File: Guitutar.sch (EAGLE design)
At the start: 16 parts

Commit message: Added headers, Bluetooth, ICSP header, and I/O connections
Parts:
- removed JP5: (no value), pinhead:PINHD-2X13
- added C8: (no value), rcl:C-USC0805
- added ICSP: (no value), pinhead:PINHD-2X3
- added LED1: (no value), led:LEDSMT1206
- added R3: (no value), rcl:R-US_M0805
- JP1: device pinhead:PINHD-2X3 -> pinhead:PINHD-1X25
- JP2, JP3, JP4: device pinhead:PINHD-2X13 -> pinhead:PINHD-1X25
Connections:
- removed net GND: C1.2, C7.1
- removed net N$11: C6.2, U$1.VSS5
- removed net N$6: C3.1, U$1.AVSS
- removed net N$8: C5.1, U$1.VSS4
- new net EAN: U$2.EAN
- new net LED: LED1.C, U$2.LED1
- new net N$15: LED1.A, R3.1
- new net N$16: R3.2, U$2.LDO33_O, U$2.VDD_IO
- new net P0_0: JP1.14, JP1.18, U$1.AN19/C2INC/RPG9/PMA2/RG9, U$1.AN32/RPE8/RE8, U$2.P0_0
- new net P0_4: JP1.3, U$1.AN22/RPE5/PMD5/RE5, U$2.P0_4
- new net P0_5: JP1.12, U$1.AN18/C2IND/RPG8/PMA3/RG8, U$2.P0_5
- new net P1_2: U$2.P1_2/SCL
- new net P1_3: U$2.P1_3/SDA
- new net P1_5: JP1.1, U$1.AN28/RG15, U$2.P1_5
- new net P1_7: JP1.19, U$1.AN33/RPE9/RE9, U$2.P1_7
- new net P2_0: U$2.P2_0
- new net P2_4: U$2.P2_4
- new net P3_1: JP1.11, U$1.AN17/C1INC/RPG7/PMA4/RG7, U$2.P3_1
- new net P3_2: JP1.10, U$1.AN16/C1IND/RPG6/SCK2/PMA5/RG6, U$2.P3_2
- new net P3_3: JP1.9, U$1.RPC4/CTED7/RC4, U$2.P3_3
- new net P3_4: JP1.8, U$1.AN31/RPC3/RC3, U$2.P3_4
- new net P3_6: U$2.P3_6
- new net P3_7: JP1.7, U$1.AN30/RPC2/RC2, U$2.P3_7
- new net PE: C1.2, C7.1, C8.2, U$2.GND, U$2.GND1
- new net RST_N: JP1.6, U$1.AN29/RPC1/RC1, U$2.RST_N
- new net RXD: JP1.21, U$1.AN4/C1INB/RB4, U$2.HCI_RXD
- new net SW_BTN: JP1.4, U$1.AN23/PMD6/RE6, U$2.SW_BTN
- new net TXD: JP1.20, U$1.AN5/C1INA/RPB5/VBUSON/RB5, U$2.HCI_TXD
- new net VSS: C2.1, C3.2, C4.2, C5.1, C6.2, JP1.15, JP2.20, JP2.6, JP3.15, JP3.25, U$1.AVSS, U$1.VSS1, U$1.VSS3, U$1.VSS4, U$1.VSS5
- new net WAKEUP: JP1.5, U$1.AN27/PMD7/RE7, U$2.WAKEUP
- net N$10: now also JP4.11
- net N$12: now also JP4.10
- net N$13: now also ICSP.1, JP1.13; no longer JP1.1
- net N$14: now also ICSP.4, JP1.25; no longer JP1.4
- net N$2: now also ICSP.5, JP1.24; no longer JP1.5
- net N$3: now also JP1.17, U$1.TMS/CTED1/RA0; no longer C2.1, U$1.VSS1
- net N$4: now also JP1.22, U$1.PGED3/AN3/C2INA/RPB3/RB3; no longer C4.2, U$1.VSS3
- net N$5: now also JP1.23, U$1.PGEC3/AN2/CTCMP/C2INB/RPB2/CTED13/RB2; no longer C2.2, C3.2, U$1.AVDD, U$1.VDD1
- net N$7: now also JP2.21
- net N$9: now also JP3.12, JP3.5
- net VDD: now also C2.2, C3.1, C8.1, JP1.16, JP1.2, JP2.5, U$1.AVDD, U$1.VDD, U$1.VDD1, U$2.BAT_IN

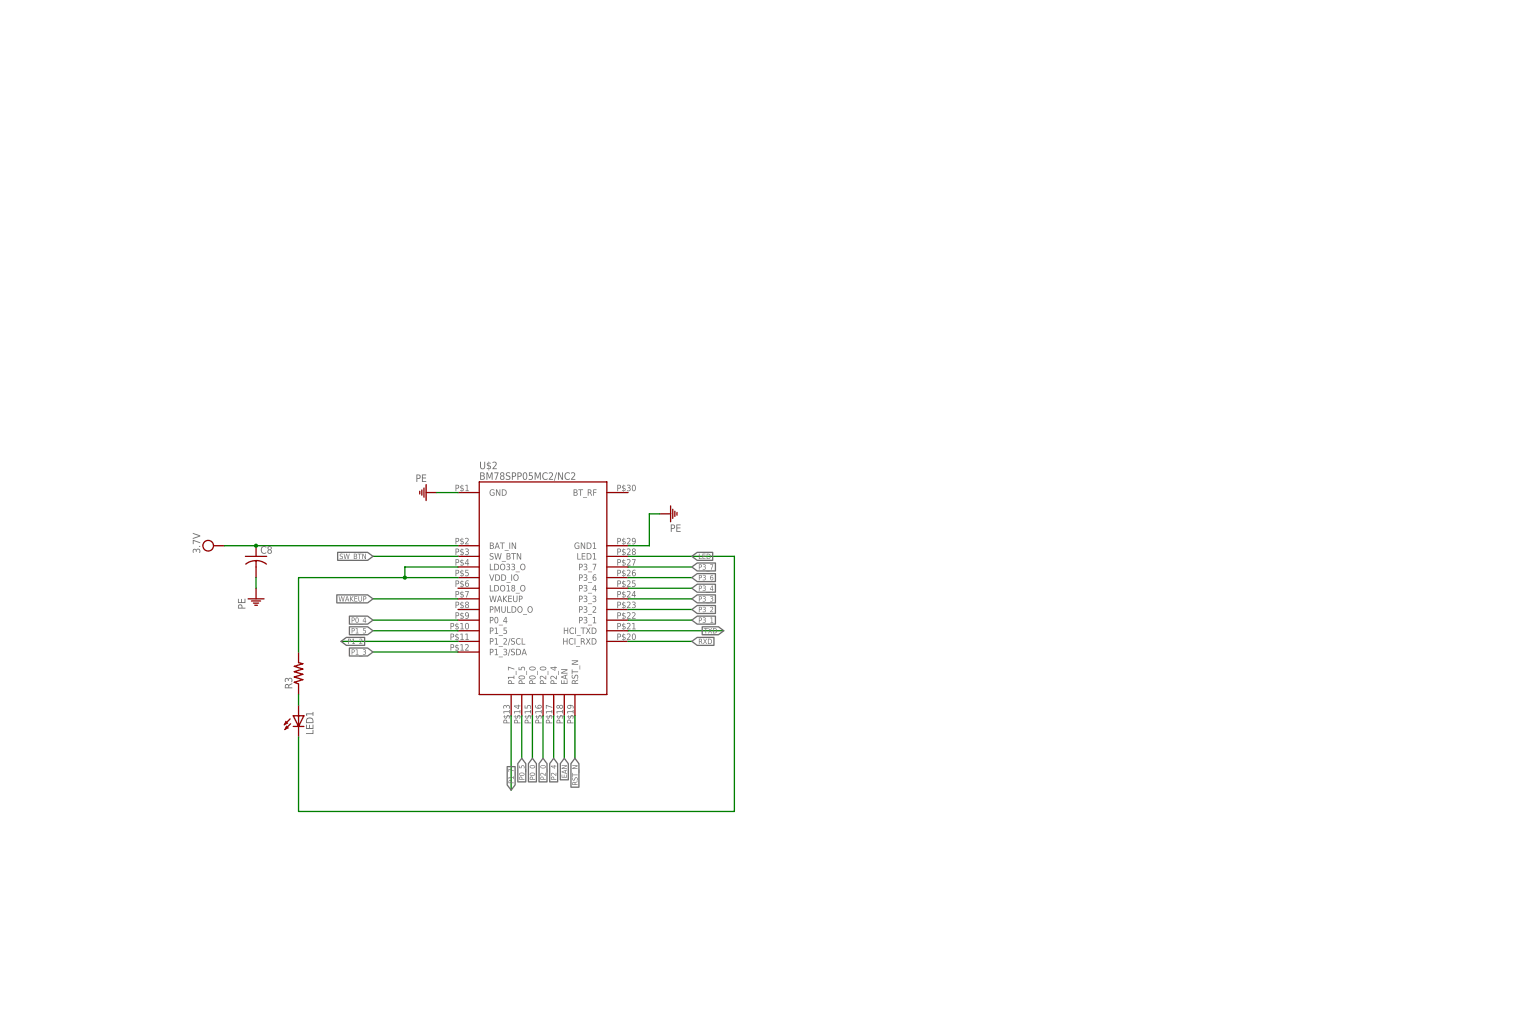
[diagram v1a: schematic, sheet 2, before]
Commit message: Added xref connections, switch matrix, and connected all MCU pins to headers
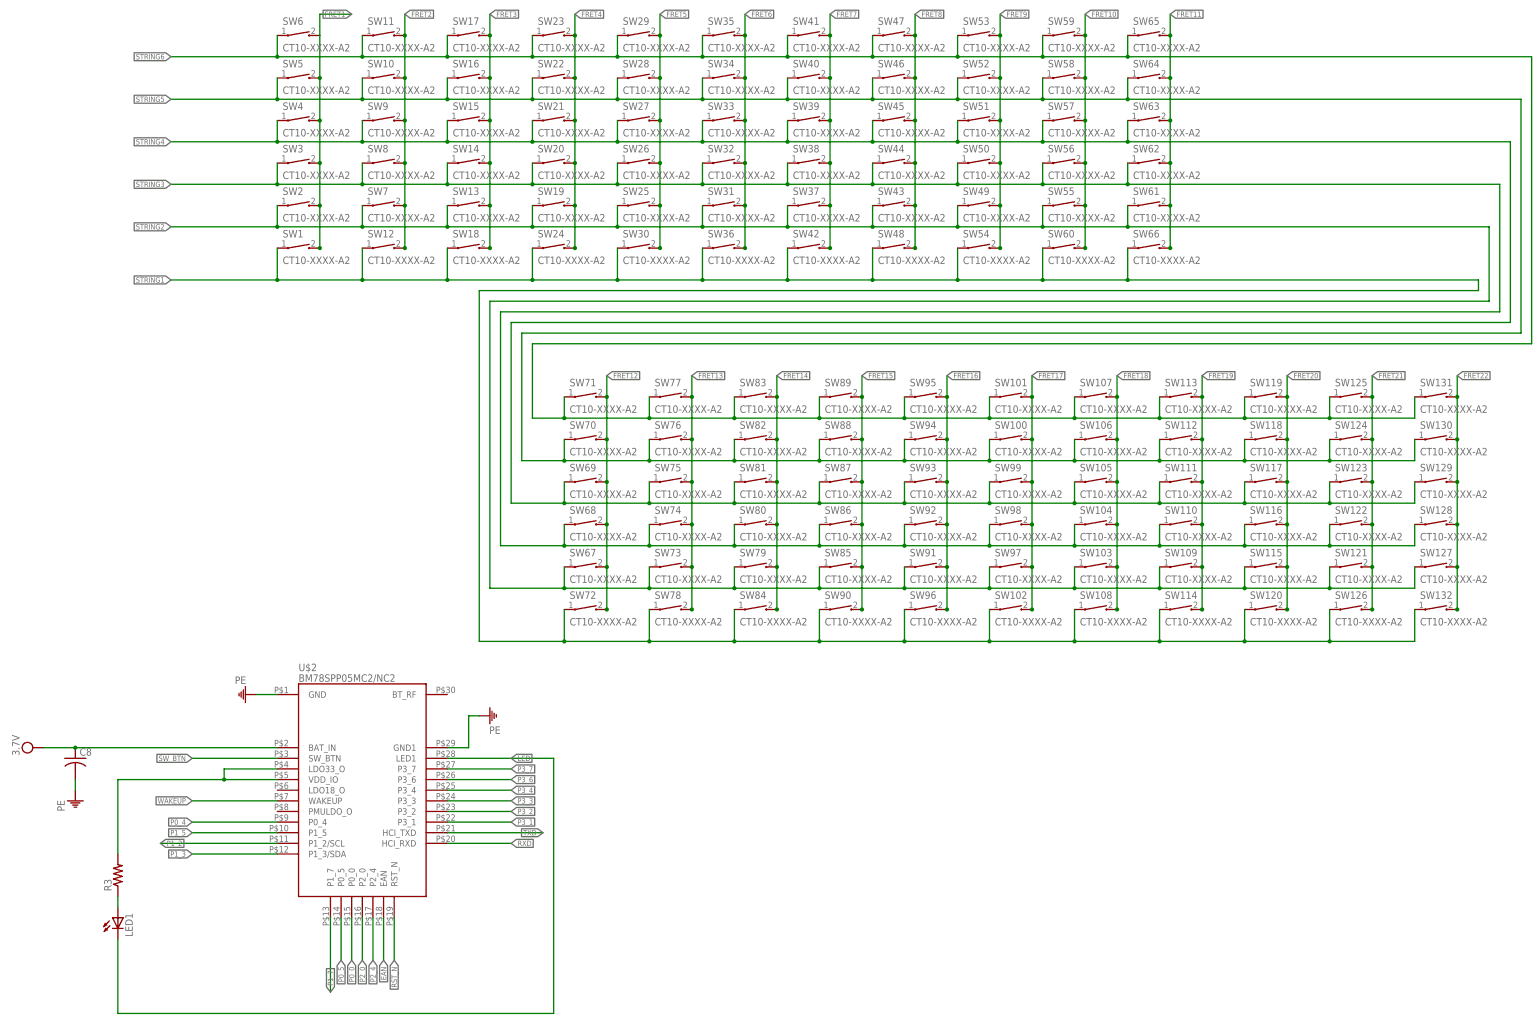
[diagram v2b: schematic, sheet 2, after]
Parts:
- added SW1, SW10, SW100, SW101, SW102, SW103, SW104, SW105, SW106, SW107, SW108, SW109, SW11, SW110, SW111, SW112, SW113, SW114, SW115, SW116, SW117, SW118, SW119, SW12, SW120, SW121, SW122, SW123, SW124, SW125, SW126, SW127, SW128, SW129, SW13, SW130, SW131, SW132, SW14, SW15, SW16, SW17, SW18, SW19, SW2, SW20, SW21, SW22, SW23, SW24, SW25, SW26, SW27, SW28, SW29, SW3, SW30, SW31, SW32, SW33, SW34, SW35, SW36, SW37, SW38, SW39, SW4, SW40, SW41, SW42, SW43, SW44, SW45, SW46, SW47, SW48, SW49, SW5, SW50, SW51, SW52, SW53, SW54, SW55, SW56, SW57, SW58, SW59, SW6, SW60, SW61, SW62, SW63, SW64, SW65, SW66, SW67, SW68, SW69, SW7, SW70, SW71, SW72, SW73, SW74, SW75, SW76, SW77, SW78, SW79, SW8, SW80, SW81, SW82, SW83, SW84, SW85, SW86, SW87, SW88, SW89, SW9, SW90, SW91, SW92, SW93, SW94, SW95, SW96, SW97, SW98, SW99: CT10-XXXX-A2, switch-coto:CT10-XXXX-A2
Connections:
- new net FRET1: JP2.16, SW1.2, SW2.2, SW3.2, SW4.2, SW5.2, SW6.2, U$1.AN12/PMA11/RB12
- new net FRET10: JP3.2, SW55.2, SW56.2, SW57.2, SW58.2, SW59.2, SW60.2, U$1.AN38/RPF2/RF2
- new net FRET11: JP3.3, SW61.2, SW62.2, SW63.2, SW64.2, SW65.2, SW66.2, U$1.AN39/RPF8/RF8
- new net FRET12: JP3.8, SW67.2, SW68.2, SW69.2, SW70.2, SW71.2, SW72.2, U$1.SCL2/RA2
- new net FRET13: JP3.9, SW73.2, SW74.2, SW75.2, SW76.2, SW77.2, SW78.2, U$1.SDA2/RA3
- new net FRET14: JP3.10, SW79.2, SW80.2, SW81.2, SW82.2, SW83.2, SW84.2, U$1.TDI/CTED9/RA4
- new net FRET15: JP3.11, SW85.2, SW86.2, SW87.2, SW88.2, SW89.2, SW90.2, U$1.TDO/RA5
- new net FRET16: JP3.13, SW91.2, SW92.2, SW93.2, SW94.2, SW95.2, SW96.2, U$1.OSC1/CLKI/RC12
- new net FRET17: JP3.14, SW100.2, SW101.2, SW102.2, SW97.2, SW98.2, SW99.2, U$1.OSC2/CLKO/RC15
- new net FRET18: JP3.16, SW103.2, SW104.2, SW105.2, SW106.2, SW107.2, SW108.2, U$1.RPA14/SCL1/RA14
- new net FRET19: JP3.17, SW109.2, SW110.2, SW111.2, SW112.2, SW113.2, SW114.2, U$1.RPA15/SDA1/RA15
- new net FRET2: JP2.17, SW10.2, SW11.2, SW12.2, SW7.2, SW8.2, SW9.2, U$1.AN13/PMA10/RB13
- new net FRET20: JP3.18, SW115.2, SW116.2, SW117.2, SW118.2, SW119.2, SW120.2, U$1.RPD8/RTCC/RD8
- new net FRET21: JP3.19, SW121.2, SW122.2, SW123.2, SW124.2, SW125.2, SW126.2, U$1.RPD9/RD9
- new net FRET22: JP3.20, SW127.2, SW128.2, SW129.2, SW130.2, SW131.2, SW132.2, U$1.RPD10/SCK1/PMA15/RD10
- new net FRET3: JP2.18, SW13.2, SW14.2, SW15.2, SW16.2, SW17.2, SW18.2, U$1.AN14/RPB14/CTED5/PMA1/RB14
- new net FRET4: JP2.19, SW19.2, SW20.2, SW21.2, SW22.2, SW23.2, SW24.2, U$1.AN15/RPB15/OCFB/CTED6/PMA0/RB15
- new net FRET5: JP2.22, SW25.2, SW26.2, SW27.2, SW28.2, SW29.2, SW30.2, U$1.AN36/RPD14/RD14
- new net FRET6: JP2.23, SW31.2, SW32.2, SW33.2, SW34.2, SW35.2, SW36.2, U$1.AN37/RPD15/SCK4/RD15
- new net FRET7: JP2.24, SW37.2, SW38.2, SW39.2, SW40.2, SW41.2, SW42.2, U$1.RPF4/PMA9/RF4
- new net FRET8: JP2.25, SW43.2, SW44.2, SW45.2, SW46.2, SW47.2, SW48.2, U$1.RPF5/PMA8/RF5
- new net FRET9: JP3.1, SW49.2, SW50.2, SW51.2, SW52.2, SW53.2, SW54.2, U$1.USBID/RPF3/RF3
- new net N$100: JP4.19, U$1.AN47/PMD1/RE1
- new net N$101: JP4.20, U$1.RG14
- new net N$102: JP4.21, U$1.RG12
- new net N$103: JP4.22, U$1.RG13
- new net N$104: JP4.23, U$1.AN20/PMD2/RE2
- new net N$105: JP4.24, U$1.RPE3/CTPLS/PMD3/RE3
- new net N$106: JP4.25, U$1.AN21/PMD4/RE4
- new net N$42: JP2.1, U$1.PGEC2/AN6/RPB6/RB6
- new net N$43: JP2.2, U$1.PGED2/AN7/RPB7/CTED3/RB7
- new net N$44: JP2.3, U$1.VREF-/PMA7/RA9
- new net N$45: JP2.4, U$1.VREF+/PMA6/RA10
- new net N$50: JP2.11, U$1.VSS2
- new net N$51: JP2.12, U$1.VDD2
- new net N$52: JP2.13, U$1.TCK/CTED2/RA1
- new net N$66: JP3.4, U$1.VBUS
- new net N$67: JP3.6, U$1.D-
- new net N$68: JP3.7, U$1.D+
- new net N$80: JP3.21, U$1.RPD11/PMA14/RD11
- new net N$81: JP3.22, U$1.RPD0/INT0/RD0
- new net N$82: JP3.23, U$1.SOSCI/RPC13/RC13
- new net N$83: JP3.24, U$1.SOSCO/RPC14/T1CK/RC14
- new net N$84: JP4.1, U$1.AN24/RPD1/RD1
- new net N$85: JP4.2, U$1.AN25/RPD2/RD2
- new net N$86: JP4.3, U$1.AN26/C3IND/RPD3/RD3
- new net N$87: JP4.4, U$1.AN40/RPD12/PMD12/RD12
- new net N$88: JP4.5, U$1.AN41/PMD13/RD13
- new net N$89: JP4.6, U$1.RPD4/PMWR/RD4
- new net N$90: JP4.7, U$1.RPD5/PMRD/RD5
- new net N$91: JP4.8, U$1.AN42/C3INC/PMD14/RD6
- new net N$92: JP4.9, U$1.AN43/C3INB/PMD15/RD7
- new net N$93: JP4.12, U$1.AN44/C3INA/RPF0/PMD11/RF0
- new net N$94: JP4.13, U$1.AN45/RPF1/PMD10/RF1
- new net N$95: JP4.14, U$1.RPG1/PMD9/RG1
- new net N$96: JP4.15, U$1.RPG0/PMD8/RG0
- new net N$97: JP4.16, U$1.RA6
- new net N$98: JP4.17, U$1.CTED8/RA7
- new net N$99: JP4.18, U$1.AN46/PMD0/RE0
- new net STRING1: JP2.7, SW1.1, SW102.1, SW108.1, SW114.1, SW12.1, SW120.1, SW126.1, SW132.1, SW18.1, SW24.1, SW30.1, SW36.1, SW42.1, SW48.1, SW54.1, SW60.1, SW66.1, SW72.1, SW78.1, SW84.1, SW90.1, SW96.1, U$1.AN8/RPB8/CTED10/RB8
- new net STRING2: JP2.8, SW103.1, SW109.1, SW115.1, SW121.1, SW127.1, SW13.1, SW19.1, SW2.1, SW25.1, SW31.1, SW37.1, SW43.1, SW49.1, SW55.1, SW61.1, SW67.1, SW7.1, SW73.1, SW79.1, SW85.1, SW91.1, SW97.1, U$1.AN9/RPB9/CTED4/RB9
- new net STRING3: JP2.9, SW104.1, SW110.1, SW116.1, SW122.1, SW128.1, SW14.1, SW20.1, SW26.1, SW3.1, SW32.1, SW38.1, SW44.1, SW50.1, SW56.1, SW62.1, SW68.1, SW74.1, SW8.1, SW80.1, SW86.1, SW92.1, SW98.1, U$1.CVREFOUT/AN10/RPB10/CTED11/PMA13/RB10
- new net STRING4: JP2.10, SW105.1, SW111.1, SW117.1, SW123.1, SW129.1, SW15.1, SW21.1, SW27.1, SW33.1, SW39.1, SW4.1, SW45.1, SW51.1, SW57.1, SW63.1, SW69.1, SW75.1, SW81.1, SW87.1, SW9.1, SW93.1, SW99.1, U$1.AN11/PMA12/RB11
- new net STRING5: JP2.14, SW10.1, SW100.1, SW106.1, SW112.1, SW118.1, SW124.1, SW130.1, SW16.1, SW22.1, SW28.1, SW34.1, SW40.1, SW46.1, SW5.1, SW52.1, SW58.1, SW64.1, SW70.1, SW76.1, SW82.1, SW88.1, SW94.1, U$1.AN34/RPF13/SCK3/RF13
- new net STRING6: JP2.15, SW101.1, SW107.1, SW11.1, SW113.1, SW119.1, SW125.1, SW131.1, SW17.1, SW23.1, SW29.1, SW35.1, SW41.1, SW47.1, SW53.1, SW59.1, SW6.1, SW65.1, SW71.1, SW77.1, SW83.1, SW89.1, SW95.1, U$1.AN35/RPF12/RF12
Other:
- moved on the sheet: C3, C4, C5, C6, C7, C8, LED1, R3, U$2

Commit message: Added LEDs and connected them to MCU. Increased size of page 2.
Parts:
- added LED10, LED100, LED101, LED102, LED103, LED104, LED105, LED106, LED107, LED108, LED109, LED11, LED110, LED111, LED112, LED113, LED114, LED115, LED116, LED117, LED118, LED119, LED12, LED120, LED121, LED122, LED123, LED124, LED125, LED126, LED127, LED128, LED129, LED13, LED130, LED131, LED132, LED133, LED134, LED135, LED136, LED137, LED138, LED139, LED14, LED15, LED16, LED17, LED18, LED19, LED2, LED20, LED21, LED22, LED23, LED24, LED25, LED26, LED27, LED28, LED29, LED3, LED30, LED31, LED32, LED33, LED34, LED35, LED36, LED37, LED38, LED39, LED4, LED40, LED41, LED42, LED43, LED44, LED45, LED46, LED47, LED48, LED49, LED5, LED50, LED51, LED52, LED53, LED54, LED55, LED56, LED57, LED58, LED59, LED6, LED60, LED61, LED62, LED63, LED64, LED65, LED66, LED67, LED68, LED69, LED7, LED70, LED71, LED72, LED73, LED74, LED75, LED76, LED77, LED78, LED79, LED8, LED80, LED81, LED82, LED83, LED84, LED85, LED86, LED87, LED88, LED89, LED9, LED90, LED91, LED92, LED93, LED94, LED95, LED96, LED97, LED98, LED99: (no value), led:LEDSMT1206
- added U$10, U$11, U$12, U$13, U$14, U$15, U$16, U$17, U$18, U$19, U$20, U$21, U$22, U$23, U$24, U$25, U$3, U$4, U$5, U$6, U$7, U$8, U$9: MM74HC595TSSOP-LD16, ECE477_Guitutar:MM74HC595TSSOP-LD16
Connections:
- removed net N$100: JP4.19, U$1.AN47/PMD1/RE1
- removed net N$101: JP4.20, U$1.RG14
- removed net N$102: JP4.21, U$1.RG12
- removed net N$103: JP4.22, U$1.RG13
- removed net N$104: JP4.23, U$1.AN20/PMD2/RE2
- removed net N$105: JP4.24, U$1.RPE3/CTPLS/PMD3/RE3
- removed net N$106: JP4.25, U$1.AN21/PMD4/RE4
- removed net N$80: JP3.21, U$1.RPD11/PMA14/RD11
- removed net N$81: JP3.22, U$1.RPD0/INT0/RD0
- removed net N$82: JP3.23, U$1.SOSCI/RPC13/RC13
- removed net N$83: JP3.24, U$1.SOSCO/RPC14/T1CK/RC14
- removed net N$84: JP4.1, U$1.AN24/RPD1/RD1
- removed net N$85: JP4.2, U$1.AN25/RPD2/RD2
- removed net N$86: JP4.3, U$1.AN26/C3IND/RPD3/RD3
- removed net N$87: JP4.4, U$1.AN40/RPD12/PMD12/RD12
- removed net N$88: JP4.5, U$1.AN41/PMD13/RD13
- removed net N$89: JP4.6, U$1.RPD4/PMWR/RD4
- removed net N$90: JP4.7, U$1.RPD5/PMRD/RD5
- removed net N$91: JP4.8, U$1.AN42/C3INC/PMD14/RD6
- removed net N$92: JP4.9, U$1.AN43/C3INB/PMD15/RD7
- removed net N$93: JP4.12, U$1.AN44/C3INA/RPF0/PMD11/RF0
- removed net N$94: JP4.13, U$1.AN45/RPF1/PMD10/RF1
- removed net N$95: JP4.14, U$1.RPG1/PMD9/RG1
- removed net N$96: JP4.15, U$1.RPG0/PMD8/RG0
- removed net N$97: JP4.16, U$1.RA6
- removed net N$98: JP4.17, U$1.CTED8/RA7
- removed net N$99: JP4.18, U$1.AN46/PMD0/RE0
- new net G: JP3.24, U$1.SOSCO/RPC14/T1CK/RC14, U$10.G, U$11.G, U$12.G, U$13.G, U$14.G, U$15.G, U$16.G, U$17.G, U$18.G, U$19.G, U$20.G, U$21.G, U$22.G, U$23.G, U$24.G, U$25.G, U$3.G, U$4.G, U$5.G, U$6.G, U$7.G, U$8.G, U$9.G
- new net GND: LED10.C, LED100.C, LED101.C, LED102.C, LED103.C, LED104.C, LED105.C, LED106.C, LED107.C, LED108.C, LED109.C, LED11.C, LED110.C, LED111.C, LED112.C, LED113.C, LED114.C, LED115.C, LED116.C, LED117.C, LED118.C, LED119.C, LED12.C, LED120.C, LED121.C, LED122.C, LED123.C, LED124.C, LED125.C, LED126.C, LED127.C, LED128.C, LED129.C, LED13.C, LED130.C, LED131.C, LED132.C, LED133.C, LED134.C, LED135.C, LED136.C, LED137.C, LED138.C, LED139.C, LED14.C, LED15.C, LED16.C, LED17.C, LED18.C, LED19.C, LED2.C, LED20.C, LED21.C, LED22.C, LED23.C, LED24.C, LED25.C, LED26.C, LED27.C, LED28.C, LED29.C, LED3.C, LED30.C, LED31.C, LED32.C, LED33.C, LED34.C, LED35.C, LED36.C, LED37.C, LED38.C, LED39.C, LED4.C, LED40.C, LED41.C, LED42.C, LED43.C, LED44.C, LED45.C, LED46.C, LED47.C, LED48.C, LED49.C, LED5.C, LED50.C, LED51.C, LED52.C, LED53.C, LED54.C, LED55.C, LED56.C, LED57.C, LED58.C, LED59.C, LED6.C, LED60.C, LED61.C, LED62.C, LED63.C, LED64.C, LED65.C, LED66.C, LED67.C, LED68.C, LED69.C, LED7.C, LED70.C, LED71.C, LED72.C, LED73.C, LED74.C, LED75.C, LED76.C, LED77.C, LED78.C, LED79.C, LED8.C, LED80.C, LED81.C, LED82.C, LED83.C, LED84.C, LED85.C, LED86.C, LED87.C, LED88.C, LED89.C, LED9.C, LED90.C, LED91.C, LED92.C, LED93.C, LED94.C, LED95.C, LED96.C, LED97.C, LED98.C, LED99.C, U$10.GND, U$11.GND, U$12.GND, U$13.GND, U$14.GND, U$15.GND, U$16.GND, U$17.GND, U$18.GND, U$19.GND, U$20.GND, U$21.GND, U$22.GND, U$23.GND, U$24.GND, U$25.GND, U$3.GND, U$4.GND, U$5.GND, U$6.GND, U$7.GND, U$8.GND, U$9.GND
- new net LED_SER1: JP4.25, U$1.AN21/PMD4/RE4, U$3.SER
- new net LED_SER10: JP4.16, U$1.RA6, U$12.SER
- new net LED_SER11: JP4.15, U$1.RPG0/PMD8/RG0, U$13.SER
- new net LED_SER12: JP4.14, U$1.RPG1/PMD9/RG1, U$14.SER
- new net LED_SER13: JP4.13, U$1.AN45/RPF1/PMD10/RF1, U$15.SER
- new net LED_SER14: JP4.12, U$1.AN44/C3INA/RPF0/PMD11/RF0, U$16.SER
- new net LED_SER15: JP4.9, U$1.AN43/C3INB/PMD15/RD7, U$17.SER
- new net LED_SER16: JP4.8, U$1.AN42/C3INC/PMD14/RD6, U$18.SER
- new net LED_SER17: JP4.7, U$1.RPD5/PMRD/RD5, U$19.SER
- new net LED_SER18: JP4.6, U$1.RPD4/PMWR/RD4, U$20.SER
- new net LED_SER19: JP4.5, U$1.AN41/PMD13/RD13, U$21.SER
- new net LED_SER2: JP4.24, U$1.RPE3/CTPLS/PMD3/RE3, U$4.SER
- new net LED_SER20: JP4.4, U$1.AN40/RPD12/PMD12/RD12, U$22.SER
- new net LED_SER21: JP4.3, U$1.AN26/C3IND/RPD3/RD3, U$23.SER
- new net LED_SER22: JP4.2, U$1.AN25/RPD2/RD2, U$24.SER
- new net LED_SER23: JP4.1, U$1.AN24/RPD1/RD1, U$25.SER
- new net LED_SER3: JP4.23, U$1.AN20/PMD2/RE2, U$5.SER
- new net LED_SER4: JP4.22, U$1.RG13, U$6.SER
- new net LED_SER5: JP4.21, U$1.RG12, U$7.SER
- new net LED_SER6: JP4.20, U$1.RG14, U$8.SER
- new net LED_SER7: JP4.19, U$1.AN47/PMD1/RE1, U$9.SER
- new net LED_SER8: JP4.18, U$1.AN46/PMD0/RE0, U$10.SER
- new net LED_SER9: JP4.17, U$1.CTED8/RA7, U$11.SER
- new net N$107: LED34.A, U$8.QD
- new net N$108: LED35.A, U$8.QE
- new net N$109: LED33.A, U$8.QC
- new net N$11: LED5.A, U$3.QE
- new net N$110: LED32.A, U$8.QB
- new net N$111: LED36.A, U$8.QF
- new net N$117: LED37.A, U$8.QA
- new net N$118: LED40.A, U$9.QD
- new net N$119: LED41.A, U$9.QE
- new net N$120: LED39.A, U$9.QC
- new net N$121: LED38.A, U$9.QB
- new net N$122: LED42.A, U$9.QF
- new net N$128: LED43.A, U$9.QA
- new net N$129: LED46.A, U$10.QD
- new net N$130: LED47.A, U$10.QE
- new net N$131: LED45.A, U$10.QC
- new net N$132: LED44.A, U$10.QB
- new net N$133: LED48.A, U$10.QF
- new net N$139: LED49.A, U$10.QA
- new net N$140: LED52.A, U$11.QD
- new net N$141: LED53.A, U$11.QE
- new net N$142: LED51.A, U$11.QC
- new net N$143: LED50.A, U$11.QB
- new net N$144: LED54.A, U$11.QF
- new net N$150: LED55.A, U$11.QA
- new net N$151: LED58.A, U$12.QD
- new net N$152: LED59.A, U$12.QE
- new net N$153: LED57.A, U$12.QC
- new net N$154: LED56.A, U$12.QB
- new net N$155: LED60.A, U$12.QF
- new net N$161: LED61.A, U$12.QA
- new net N$162: LED64.A, U$13.QD
- new net N$163: LED65.A, U$13.QE
- new net N$164: LED63.A, U$13.QC
- new net N$165: LED62.A, U$13.QB
- new net N$166: LED66.A, U$13.QF
- new net N$17: LED3.A, U$3.QC
- new net N$172: LED67.A, U$13.QA
- new net N$173: LED70.A, U$14.QD
- new net N$174: LED71.A, U$14.QE
- new net N$175: LED69.A, U$14.QC
- new net N$176: LED68.A, U$14.QB
- new net N$177: LED72.A, U$14.QF
- new net N$18: LED2.A, U$3.QB
- new net N$183: LED73.A, U$14.QA
- new net N$184: LED76.A, U$15.QD
- new net N$185: LED77.A, U$15.QE
- new net N$186: LED75.A, U$15.QC
- new net N$187: LED74.A, U$15.QB
- new net N$188: LED78.A, U$15.QF
- new net N$19: LED6.A, U$3.QF
- new net N$194: LED79.A, U$15.QA
- new net N$195: LED82.A, U$16.QD
- new net N$196: LED83.A, U$16.QE
- new net N$197: LED81.A, U$16.QC
- new net N$198: LED80.A, U$16.QB
- new net N$199: LED84.A, U$16.QF
- new net N$205: LED85.A, U$16.QA
- new net N$206: LED88.A, U$17.QD
- new net N$207: LED89.A, U$17.QE
- new net N$208: LED87.A, U$17.QC
- new net N$209: LED86.A, U$17.QB
- new net N$210: LED90.A, U$17.QF
- new net N$216: LED91.A, U$17.QA
- new net N$217: LED94.A, U$18.QD
- new net N$218: LED95.A, U$18.QE
- new net N$219: LED93.A, U$18.QC
- new net N$220: LED92.A, U$18.QB
- new net N$221: LED96.A, U$18.QF
- new net N$227: LED97.A, U$18.QA
- new net N$228: LED100.A, U$19.QD
- new net N$229: LED101.A, U$19.QE
- new net N$230: LED99.A, U$19.QC
- new net N$231: LED98.A, U$19.QB
- new net N$232: LED102.A, U$19.QF
- new net N$238: LED103.A, U$19.QA
- new net N$239: LED106.A, U$20.QD
- new net N$240: LED107.A, U$20.QE
- new net N$241: LED105.A, U$20.QC
- new net N$242: LED104.A, U$20.QB
- new net N$243: LED108.A, U$20.QF
- new net N$249: LED109.A, U$20.QA
- new net N$250: LED112.A, U$21.QD
- new net N$251: LED113.A, U$21.QE
- new net N$252: LED111.A, U$21.QC
- new net N$253: LED110.A, U$21.QB
- new net N$254: LED114.A, U$21.QF
- new net N$26: LED10.A, U$4.QD
- new net N$260: LED115.A, U$21.QA
- new net N$261: LED118.A, U$22.QD
- new net N$262: LED119.A, U$22.QE
- new net N$263: LED117.A, U$22.QC
- new net N$264: LED116.A, U$22.QB
- new net N$265: LED120.A, U$22.QF
- new net N$27: LED11.A, U$4.QE
- new net N$271: LED121.A, U$22.QA
- new net N$272: LED124.A, U$23.QD
- new net N$273: LED125.A, U$23.QE
- new net N$274: LED123.A, U$23.QC
- new net N$275: LED122.A, U$23.QB
- new net N$276: LED126.A, U$23.QF
- new net N$28: LED9.A, U$4.QC
- new net N$282: LED127.A, U$23.QA
- new net N$283: LED130.A, U$24.QD
- new net N$284: LED131.A, U$24.QE
- new net N$285: LED129.A, U$24.QC
- new net N$286: LED128.A, U$24.QB
- new net N$287: LED132.A, U$24.QF
- new net N$29: LED8.A, U$4.QB
- new net N$293: LED133.A, U$24.QA
- new net N$294: LED136.A, U$25.QD
- new net N$295: LED137.A, U$25.QE
- new net N$296: LED135.A, U$25.QC
- new net N$297: LED134.A, U$25.QB
- new net N$298: LED138.A, U$25.QF
- new net N$30: LED12.A, U$4.QF
- new net N$304: LED139.A, U$25.QA
- new net N$36: LED13.A, U$4.QA
- new net N$37: LED16.A, U$5.QD
- new net N$38: LED17.A, U$5.QE
- new net N$39: LED15.A, U$5.QC
- new net N$40: LED14.A, U$5.QB
- new net N$41: LED18.A, U$5.QF
- new net N$54: LED19.A, U$5.QA
- new net N$55: LED22.A, U$6.QD
- new net N$56: LED23.A, U$6.QE
- new net N$57: LED21.A, U$6.QC
- new net N$58: LED20.A, U$6.QB
- new net N$59: LED24.A, U$6.QF
- new net N$6: LED7.A, U$3.QA
- new net N$65: LED25.A, U$6.QA
- new net N$69: LED28.A, U$7.QD
- new net N$70: LED29.A, U$7.QE
- new net N$71: LED27.A, U$7.QC
- new net N$72: LED26.A, U$7.QB
- new net N$73: LED30.A, U$7.QF
- new net N$79: LED31.A, U$7.QA
- new net N$8: LED4.A, U$3.QD
- new net RCK: JP3.23, U$1.SOSCI/RPC13/RC13, U$10.RCK, U$11.RCK, U$12.RCK, U$13.RCK, U$14.RCK, U$15.RCK, U$16.RCK, U$17.RCK, U$18.RCK, U$19.RCK, U$20.RCK, U$21.RCK, U$22.RCK, U$23.RCK, U$24.RCK, U$25.RCK, U$3.RCK, U$4.RCK, U$5.RCK, U$6.RCK, U$7.RCK, U$8.RCK, U$9.RCK
- new net SCK: JP3.22, U$1.RPD0/INT0/RD0, U$10.SCK, U$11.SCK, U$12.SCK, U$13.SCK, U$14.SCK, U$15.SCK, U$16.SCK, U$17.SCK, U$18.SCK, U$19.SCK, U$20.SCK, U$21.SCK, U$22.SCK, U$23.SCK, U$24.SCK, U$25.SCK, U$3.SCK, U$4.SCK, U$5.SCK, U$6.SCK, U$7.SCK, U$8.SCK, U$9.SCK
- new net SCLR: JP3.21, U$1.RPD11/PMA14/RD11, U$10.SCLR, U$11.SCLR, U$12.SCLR, U$13.SCLR, U$14.SCLR, U$15.SCLR, U$16.SCLR, U$17.SCLR, U$18.SCLR, U$19.SCLR, U$20.SCLR, U$21.SCLR, U$22.SCLR, U$23.SCLR, U$24.SCLR, U$25.SCLR, U$3.SCLR, U$4.SCLR, U$5.SCLR, U$6.SCLR, U$7.SCLR, U$8.SCLR, U$9.SCLR
- new net VCC: U$10.VCC, U$11.VCC, U$12.VCC, U$13.VCC, U$14.VCC, U$15.VCC, U$16.VCC, U$17.VCC, U$18.VCC, U$19.VCC, U$20.VCC, U$21.VCC, U$22.VCC, U$23.VCC, U$24.VCC, U$25.VCC, U$3.VCC, U$4.VCC, U$5.VCC, U$6.VCC, U$7.VCC, U$8.VCC, U$9.VCC
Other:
- moved on the sheet: C8, LED1, R3, SW1, SW10, SW100, SW101, SW102, SW103, SW104, SW105, SW106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
